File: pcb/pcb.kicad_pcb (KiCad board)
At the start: 2 copper layers, 63.8 x 43.2 mm, 34 parts, among them J1 BAT+, J10 GRN, J11 RED, J12 Load Cell, J2 BAT-, J3 Battery, J4 DS18B20, J5 TMP+, J6 TMPO, J7 TMP-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

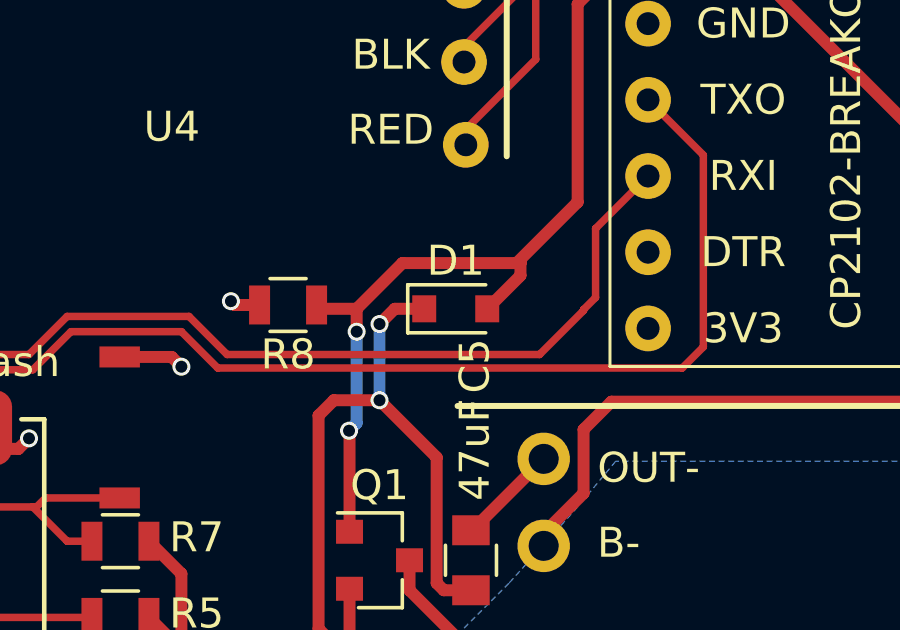
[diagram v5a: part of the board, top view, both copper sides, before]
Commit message: Switch to 1206 footprint for Schottky diode; 0805 seems hard to find
At least at the rated power we need (up to about 500ma).
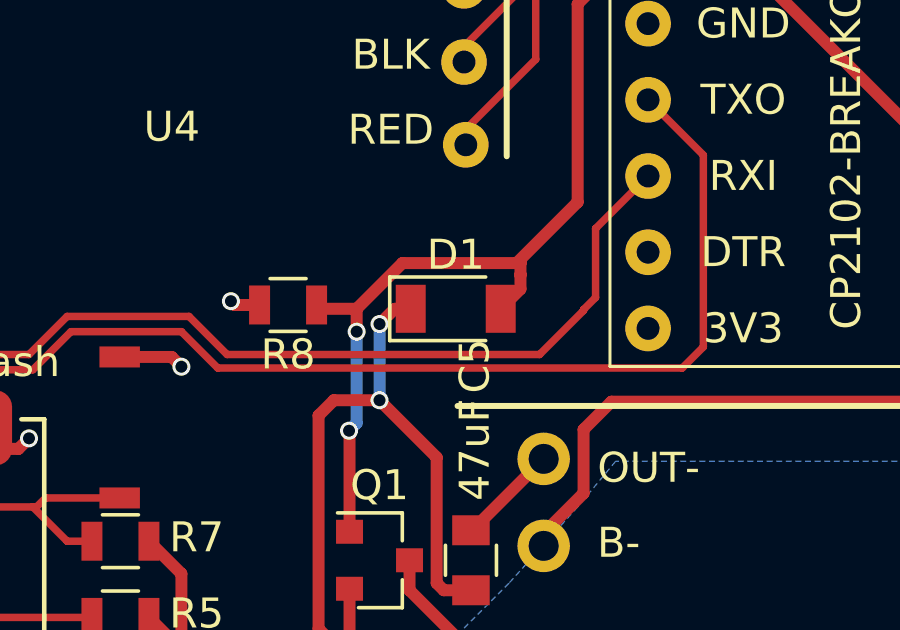
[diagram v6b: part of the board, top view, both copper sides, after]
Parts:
- D1: footprint Diodes_SMD:D_0805 -> Diodes_SMD:D_1206
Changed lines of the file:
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@@
     (links 66)
     (no_connects 0)
-    (area 99.863999 58.638 182.188 114.438001)
+    (area 106.162999 65.462999 170.113001 108.813001)
     (thickness 1.6)
     (drawings 21)
-    (tracks 382)
+    (tracks 384)
     (zones 0)
     (modules 34)
@@
   )
   (setup
-    (last_trace_width 0.25)
+    (last_trace_width 0.4)
     (user_trace_width 0.4)
     (trace_clearance 0.2)
@@
     )
   )
-  (module Diodes_SMD:D_0805 (layer F.Cu)
-    (at 138.176 86.614)
-    (descr "Diode SMD in 0805 package http://datasheets.avx.com/schottky.pdf")
-    (tags "smd diode")
-    (attr smd)
-    (fp_text reference D1 (at 0 -1.6) (layer F.SilkS)
-      (effects (font (size 1 1) (thickness 0.15)))
-    )
-    (fp_text value D_Schottky (at 0.127 -2.794) (layer F.Fab)
-      (effects (font (size 1 1) (thickness 0.15)))
-    )
-    (fp_text user %R (at 0 -1.6) (layer F.Fab)
-      (effects (font (size 1 1) (thickness 0.15)))
-    )
-    (fp_line (start -1.6 -0.8) (end -1.6 0.8) (layer F.SilkS) (width 0.12))
-    (fp_line (start -1.7 0.88) (end -1.7 -0.88) (layer F.CrtYd) (width 0.05))
-    (fp_line (start 1.7 0.88) (end -1.7 0.88) (layer F.CrtYd) (width 0.05))
-    (fp_line (start 1.7 -0.88) (end 1.7 0.88) (layer F.CrtYd) (width 0.05))
-    (fp_line (start -1.7 -0.88) (end 1.7 -0.88) (layer F.CrtYd) (width 0.05))
-    (fp_line (start 0.2 0) (end 0.4 0) (layer F.Fab) (width 0.1))
-    (fp_line (start -0.1 0) (end -0.3 0) (layer F.Fab) (width 0.1))
-    (fp_line (start -0.1 -0.2) (end -0.1 0.2) (layer F.Fab) (width 0.1))
-    (fp_line (start 0.2 0.2) (end 0.2 -0.2) (layer F.Fab) (width 0.1))
-    (fp_line (start -0.1 0) (end 0.2 0.2) (layer F.Fab) (width 0.1))
-    (fp_line (start 0.2 -0.2) (end -0.1 0) (layer F.Fab) (width 0.1))
-    (fp_line (start -1 0.65) (end -1 -0.65) (layer F.Fab) (width 0.1))
-    (fp_line (start 1 0.65) (end -1 0.65) (layer F.Fab) (width 0.1))
-    (fp_line (start 1 -0.65) (end 1 0.65) (layer F.Fab) (width 0.1))
-    (fp_line (start -1 -0.65) (end 1 -0.65) (layer F.Fab) (width 0.1))
-    (fp_line (start -1.6 0.8) (end 1 0.8) (layer F.SilkS) (width 0.12))
-    (fp_line (start -1.6 -0.8) (end 1 -0.8) (layer F.SilkS) (width 0.12))
-    (pad 1 smd rect (at -1.05 0) (size 0.8 0.9) (layers F.Cu F.Paste F.Mask)
-      (net 24 /VREG+))
-    (pad 2 smd rect (at 1.05 0) (size 0.8 0.9) (layers F.Cu F.Paste F.Mask)
-      (net 11 /USB+))
-    (model ${KISYS3DMOD}/Diodes_SMD.3dshapes/D_0805.wrl
-      (at (xyz 0 0 0))
-      (scale (xyz 1 1 1))
-      (rotate (xyz 0 0 0))
-    )
-  )
   (module TO_SOT_Packages_SMD:SOT-23 (layer F.Cu)
     (at 135.636 94.996)
@@
       (net 10 /GND))
     (model ${KISYS3DMOD}/Resistors_SMD.3dshapes/R_0805.wrl
+      (at (xyz 0 0 0))
+      (scale (xyz 1 1 1))
+      (rotate (xyz 0 0 0))
+    )
+  )
+  (module Diodes_SMD:D_1206 (layer F.Cu)
+    (at 138.176 86.614)
+    (descr "Diode SMD 1206, reflow soldering http://datasheets.avx.com/schottky.pdf")
+    (tags "Diode 1206")
+    (attr smd)
+    (fp_text reference D1 (at 0 -1.8) (layer F.SilkS)
+      (effects (font (size 1 1) (thickness 0.15)))
+    )
+    (fp_text value D_Schottky (at 0 1.9) (layer F.Fab)
+      (effects (font (size 1 1) (thickness 0.15)))
+    )
+    (fp_text user %R (at 0 -1.8) (layer F.Fab)
+      (effects (font (size 1 1) (thickness 0.15)))
+    )
+    (fp_line (start -0.254 -0.254) (end -0.254 0.254) (layer F.Fab) (width 0.1))
+    (fp_line (start 0.127 0) (end 0.381 0) (layer F.Fab) (width 0.1))
+    (fp_line (start -0.254 0) (end -0.508 0) (layer F.Fab) (width 0.1))
+    (fp_line (start 0.127 0.254) (end -0.254 0) (layer F.Fab) (width 0.1))
+    (fp_line (start 0.127 -0.254) (end 0.127 0.254) (layer F.Fab) (width 0.1))
+    (fp_line (start -0.254 0) (end 0.127 -0.254) (layer F.Fab) (width 0.1))
+    (fp_line (start -2.2 -1.06) (end -2.2 1.06) (layer F.SilkS) (width 0.12))
+    (fp_line (start -1.7 0.95) (end -1.7 -0.95) (layer F.Fab) (width 0.1))
+    (fp_line (start 1.7 0.95) (end -1.7 0.95) (layer F.Fab) (width 0.1))
+    (fp_line (start 1.7 -0.95) (end 1.7 0.95) (layer F.Fab) (width 0.1))
+    (fp_line (start -1.7 -0.95) (end 1.7 -0.95) (layer F.Fab) (width 0.1))
+    (fp_line (start -2.3 -1.16) (end 2.3 -1.16) (layer F.CrtYd) (width 0.05))
+    (fp_line (start -2.3 1.16) (end 2.3 1.16) (layer F.CrtYd) (width 0.05))
+    (fp_line (start -2.3 -1.16) (end -2.3 1.16) (layer F.CrtYd) (width 0.05))
+    (fp_line (start 2.3 -1.16) (end 2.3 1.16) (layer F.CrtYd) (width 0.05))
+    (fp_line (start 1 -1.06) (end -2.2 -1.06) (layer F.SilkS) (width 0.12))
+    (fp_line (start -2.2 1.06) (end 1 1.06) (layer F.SilkS) (width 0.12))
+    (pad 1 smd rect (at -1.5 0) (size 1 1.6) (layers F.Cu F.Paste F.Mask)
+      (net 24 /VREG+))
+    (pad 2 smd rect (at 1.5 0) (size 1 1.6) (layers F.Cu F.Paste F.Mask)
+      (net 11 /USB+))
+    (model ${KISYS3DMOD}/Diodes_SMD.3dshapes/D_1206.wrl
       (at (xyz 0 0 0))
       (scale (xyz 1 1 1))
@@
   (segment (start 110.838 70.438) (end 111.738 70.438) (width 0.4) (layer F.Cu) (net 10) (status 10))
   (segment (start 111.738 70.438) (end 112.471 71.171) (width 0.4) (layer F.Cu) (net 10))
+  (segment (start 140.335 85.471) (end 140.335 85.955) (width 0.4) (layer F.Cu) (net 11))
+  (segment (start 140.335 85.955) (end 139.676 86.614) (width 0.4) (layer F.Cu) (net 11) (status 800000))
   (segment (start 134.874 86.614) (end 133.665 86.614) (width 0.4) (layer F.Cu) (net 11))
   (segment (start 133.665 86.614) (end 133.538 86.487) (width 0.4) (layer F.Cu) (net 11))
@@
   (via (at 134.62 90.678) (size 0.6) (drill 0.4) (layers F.Cu B.Cu) (net 11))
   (segment (start 134.874 90.424) (end 134.62 90.678) (width 0.4) (layer B.Cu) (net 11))
-  (segment (start 140.335 85.09) (end 140.335 85.505) (width 0.4) (layer F.Cu) (net 11))
-  (segment (start 140.335 85.505) (end 139.226 86.614) (width 0.4) (layer F.Cu) (net 11))
+  (segment (start 140.335 85.09) (end 140.335 85.471) (width 0.4) (layer F.Cu) (net 11))
+  (segment (start 140.335 85.471) (end 140.335 85.505) (width 0.4) (layer F.Cu) (net 11))
   (segment (start 144.588 74.568) (end 144.126 74.568) (width 0.4) (layer F.Cu) (net 11))
   (segment (start 144.126 74.568) (end 142.24 76.454) (width 0.4) (layer F.Cu) (net 11))
@@
   (segment (start 111.379 78.359) (end 113.411 78.359) (width 0.25) (layer B.Cu) (net 23))
   (segment (start 118.839 105.283) (end 118.839 106.139) (width 0.25) (layer F.Cu) (net 23) (status 30))
+  (segment (start 136.676 86.614) (end 136.144 86.614) (width 0.4) (layer F.Cu) (net 24) (status 400000))
+  (via (at 135.636 89.662) (size 0.6) (drill 0.4) (layers F.Cu B.Cu) (net 24))
+  (segment (start 135.636 87.122) (end 135.636 89.662) (width 0.4) (layer B.Cu) (net 24))
+  (via (at 135.636 87.122) (size 0.6) (drill 0.4) (layers F.Cu B.Cu) (net 24))
+  (segment (start 136.144 86.614) (end 135.636 87.122) (width 0.4) (layer F.Cu) (net 24))
   (segment (start 138.684 95.996) (end 137.779 95.996) (width 0.4) (layer F.Cu) (net 24))
   (segment (start 137.541 91.567) (end 135.636 89.662) (width 0.4) (layer F.Cu) (net 24))
@@
   (segment (start 137.779 95.996) (end 137.541 95.758) (width 0.4) (layer F.Cu) (net 24))
   (segment (start 134.636 98.298) (end 134.62 98.298) (width 0.4) (layer F.Cu) (net 24))
-  (segment (start 136.144 86.614) (end 137.126 86.614) (width 0.4) (layer F.Cu) (net 24))
-  (segment (start 135.636 87.122) (end 136.144 86.614) (width 0.4) (layer F.Cu) (net 24))
-  (via (at 135.636 87.122) (size 0.6) (drill 0.4) (layers F.Cu B.Cu) (net 24))
-  (segment (start 135.636 89.662) (end 135.636 87.122) (width 0.4) (layer B.Cu) (net 24))
-  (via (at 135.636 89.662) (size 0.6) (drill 0.4) (layers F.Cu B.Cu) (net 24))
   (segment (start 134.112 89.662) (end 135.636 89.662) (width 0.4) (layer F.Cu) (net 24))
   (segment (start 133.604 90.17) (end 134.112 89.662) (width 0.4) (layer F.Cu) (net 24))

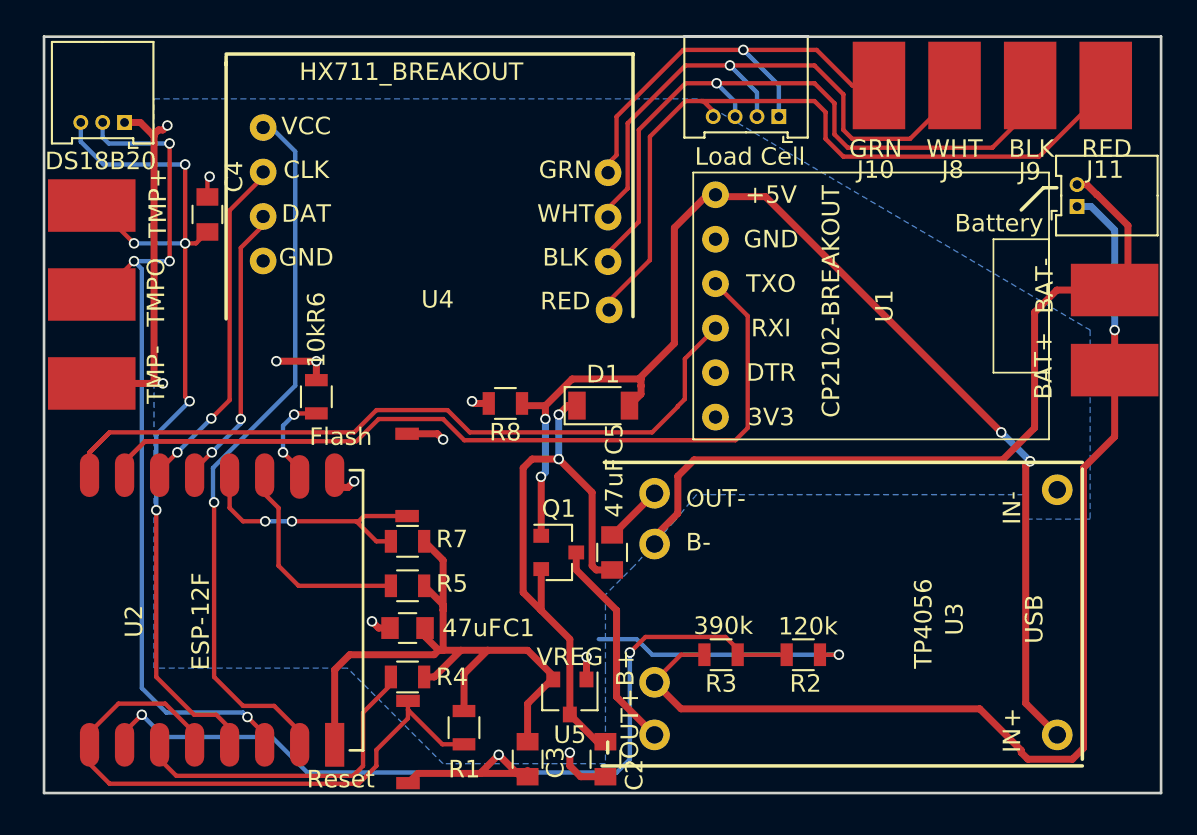
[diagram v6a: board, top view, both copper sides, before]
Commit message: Use correct diode SMD package (DO-214AC/SMA)
That's the package all the high-power ones seem to come in.
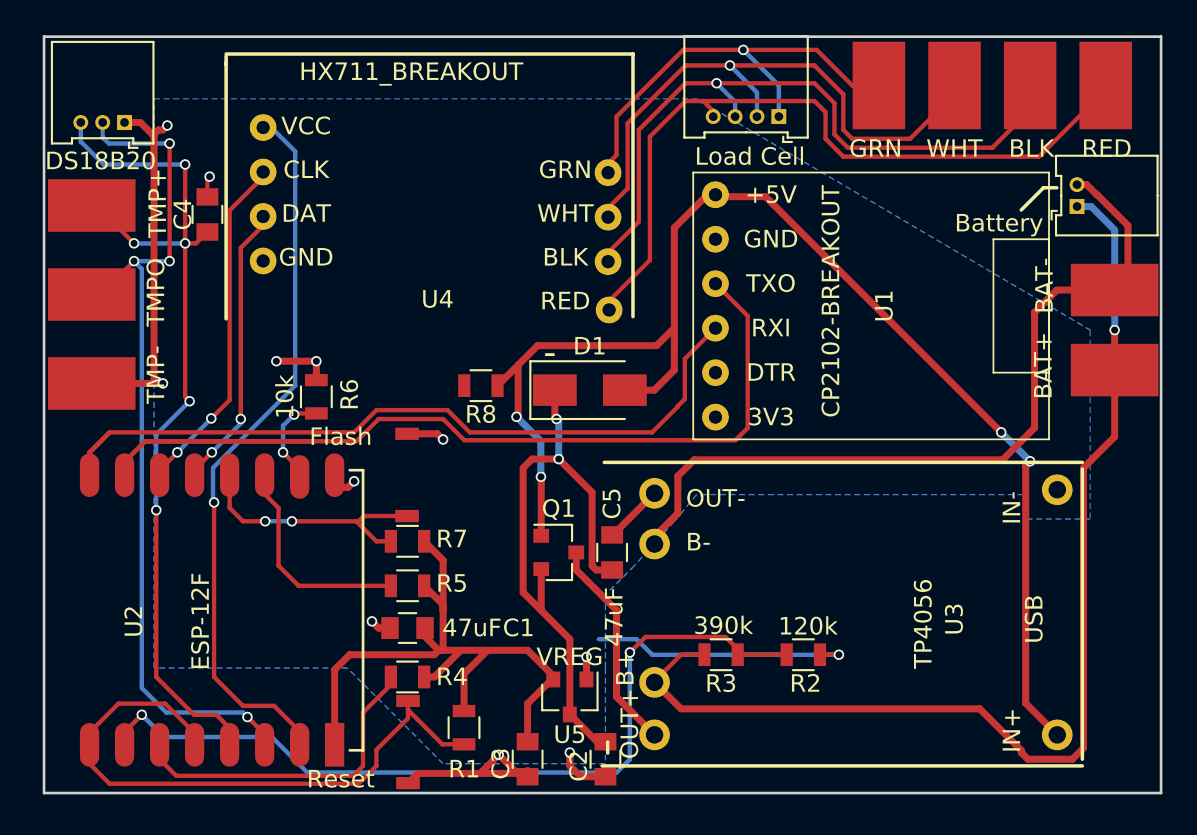
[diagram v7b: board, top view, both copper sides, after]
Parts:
- D1: footprint Diodes_SMD:D_1206 -> Diodes_SMD:D_SMA
- moved R8 1.73 mm to (131.2, 85.5)
- moved D1 1.17 mm to (137.4, 85.7)
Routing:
- net /USB+: track 70.3 -> 77.3 mm
- net /GND: track 65.9 -> 64.9 mm, vias 13 -> 12
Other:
- board text added: "-"

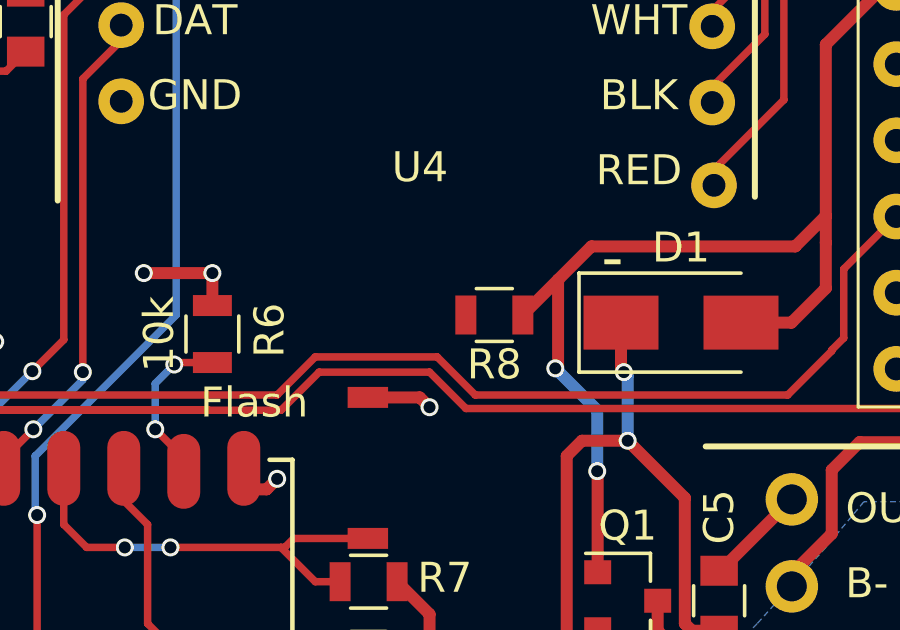
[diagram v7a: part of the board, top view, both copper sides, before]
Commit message: Fix unconnected pad
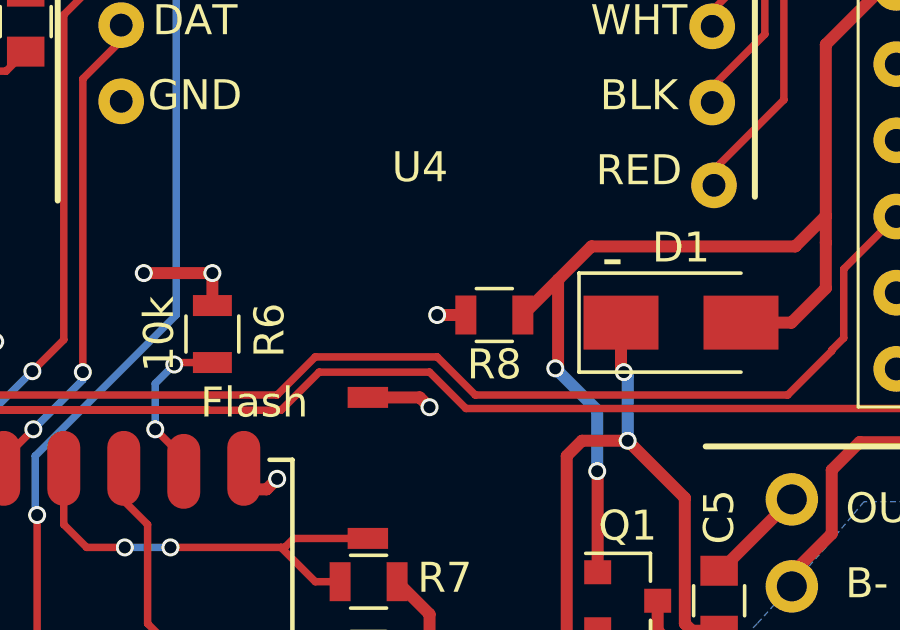
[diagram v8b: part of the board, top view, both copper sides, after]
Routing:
- net /GND: track 64.9 -> 65.9 mm, vias 12 -> 13
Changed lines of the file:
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@@
   (general
     (links 66)
-    (no_connects 1)
-    (area 106.162999 65.462999 170.113001 108.813001)
+    (no_connects 0)
+    (area 99.863999 58.638 182.188 114.438001)
     (thickness 1.6)
     (drawings 22)
-    (tracks 381)
+    (tracks 383)
     (zones 0)
     (modules 34)
@@
   (segment (start 136.636 95.996) (end 138.938 98.298) (width 0.4) (layer F.Cu) (net 9))
   (segment (start 141.108 105.416) (end 141.108 105.294) (width 0.4) (layer F.Cu) (net 9))
+  (segment (start 130.241 85.471) (end 129.286 85.471) (width 0.4) (layer F.Cu) (net 10) (status 400000))
+  (via (at 129.286 85.471) (size 0.6) (drill 0.4) (layers F.Cu B.Cu) (net 10))
   (segment (start 131.142 107.618) (end 133.669 107.618) (width 0.4) (layer F.Cu) (net 10))
   (segment (start 133.669 107.618) (end 133.858 107.807) (width 0.4) (layer F.Cu) (net 10))
@@
   (segment (start 142.24 82.169) (end 141.224 83.185) (width 0.4) (layer F.Cu) (net 11))
   (segment (start 134.427 83.185) (end 133.317 84.295) (width 0.4) (layer F.Cu) (net 11))
-  (segment (start 133.317 84.295) (end 132.141 85.471) (width 0.4) (layer F.Cu) (net 11) (status 800000))
+  (segment (start 133.317 84.295) (end 132.141 85.471) (width 0.4) (layer F.Cu) (net 11))
   (segment (start 141.224 83.185) (end 134.427 83.185) (width 0.4) (layer F.Cu) (net 11))
   (segment (start 142.24 83.058) (end 142.24 84.582) (width 0.4) (layer F.Cu) (net 11))
@@
   (segment (start 142.24 82.169) (end 142.24 83.058) (width 0.4) (layer F.Cu) (net 11))
   (segment (start 144.126 74.568) (end 142.24 76.454) (width 0.4) (layer F.Cu) (net 11))
-  (segment (start 141.097 85.725) (end 139.414 85.725) (width 0.4) (layer F.Cu) (net 11) (status 800000))
+  (segment (start 141.097 85.725) (end 139.414 85.725) (width 0.4) (layer F.Cu) (net 11))
   (segment (start 142.24 84.582) (end 141.097 85.725) (width 0.4) (layer F.Cu) (net 11))
   (segment (start 134.636 90.694) (end 134.636 94.046) (width 0.4) (layer F.Cu) (net 11))
@@
   (segment (start 111.379 78.359) (end 113.411 78.359) (width 0.25) (layer B.Cu) (net 23))
   (segment (start 118.839 105.283) (end 118.839 106.139) (width 0.25) (layer F.Cu) (net 23) (status 30))
-  (segment (start 135.414 85.725) (end 135.414 87.281) (width 0.4) (layer F.Cu) (net 24) (status 400000))
+  (segment (start 135.414 85.725) (end 135.414 87.281) (width 0.4) (layer F.Cu) (net 24))
   (via (at 135.636 89.662) (size 0.6) (drill 0.4) (layers F.Cu B.Cu) (net 24))
   (segment (start 135.636 87.503) (end 135.636 89.662) (width 0.4) (layer B.Cu) (net 24))
